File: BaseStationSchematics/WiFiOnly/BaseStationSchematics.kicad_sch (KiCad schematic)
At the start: 9 parts, among them U1 DOIT-ESP32-DEVKIT-V1, U2 Ra01_Breakout_Module-Ra01_Bre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, U3 LM386N based audio amplifier

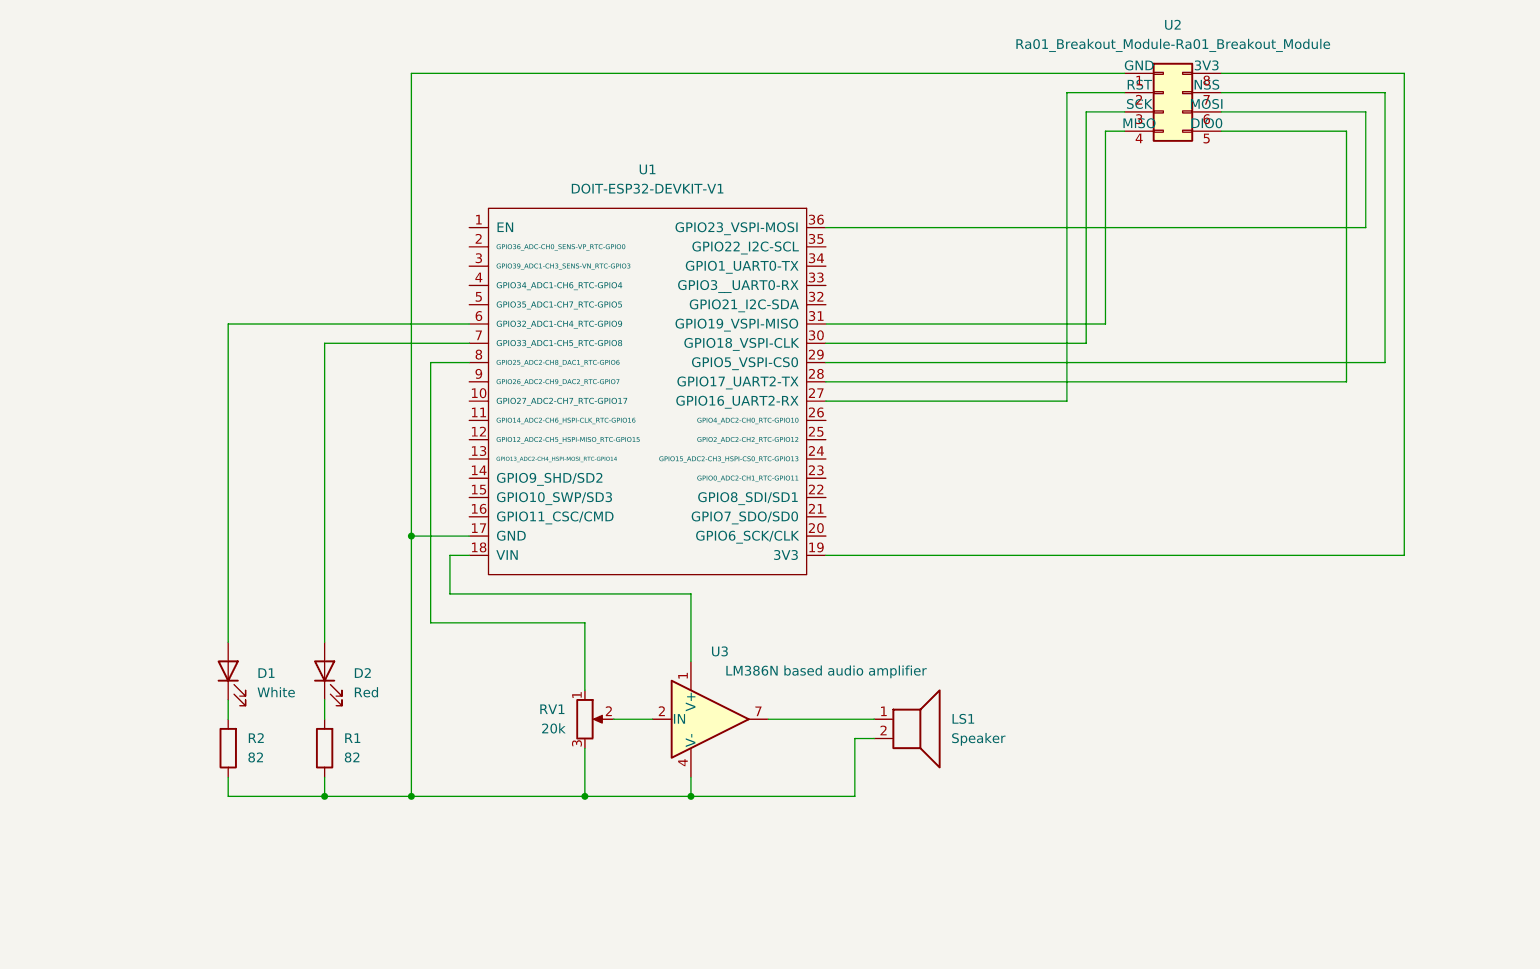
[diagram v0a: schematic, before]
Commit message: Added barometer and local timeseries
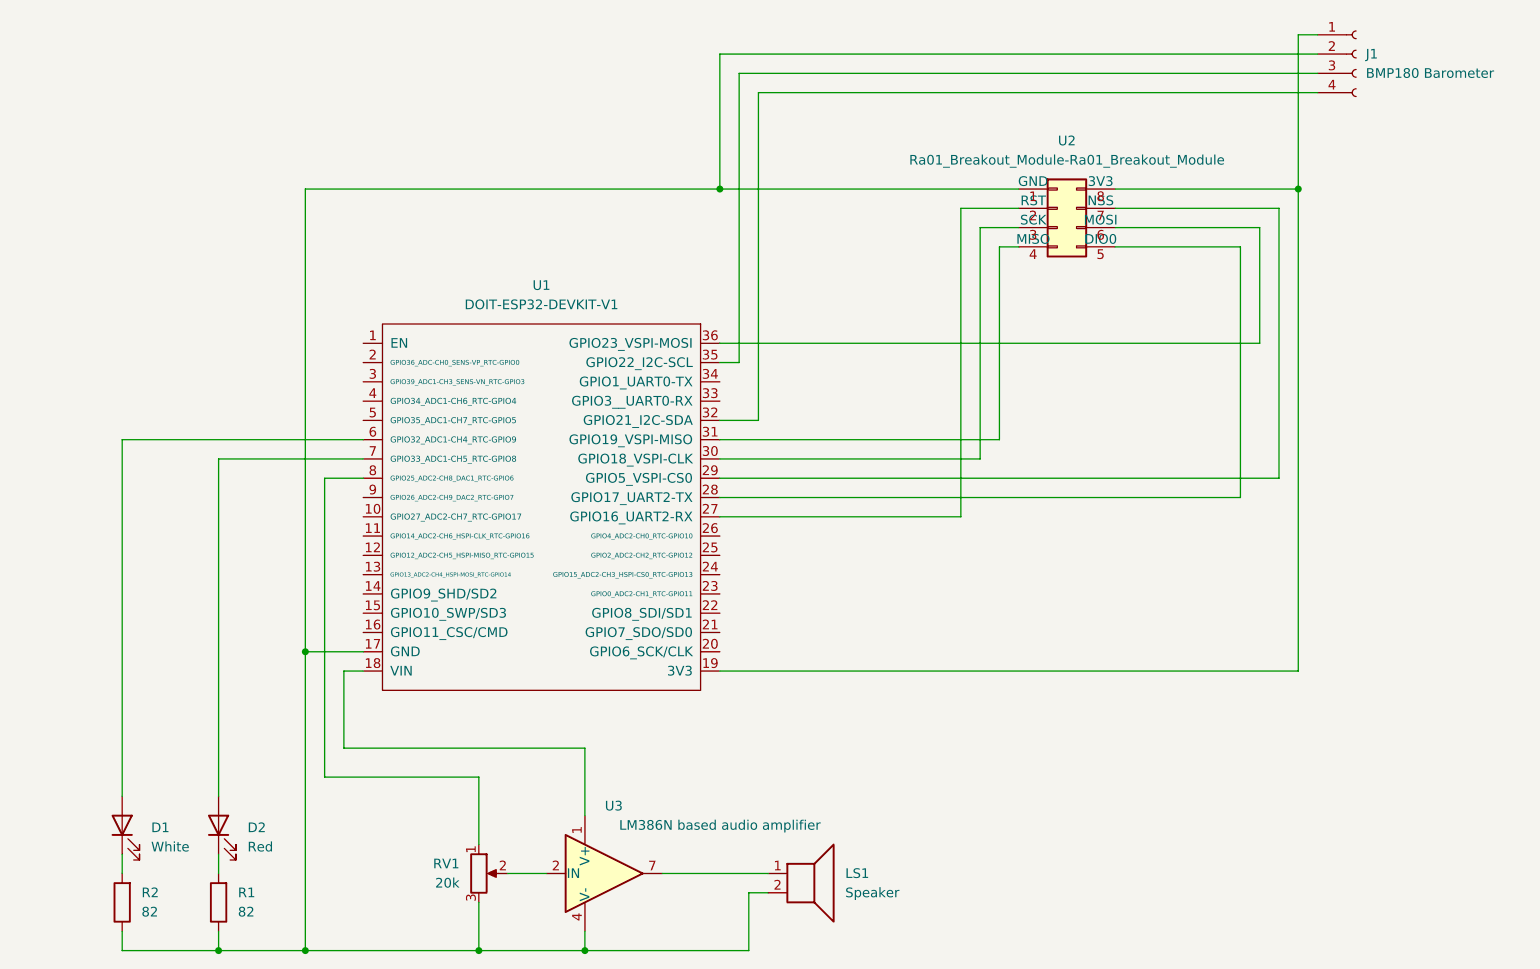
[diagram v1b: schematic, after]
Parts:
- added J1: BMP180 Barometer, symbol Connector:Conn_01x04_Socket
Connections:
- net at LS1.2, R1.1, R2.1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: now also J1.2 (Pin_2)
- net at U1.19 (3V3), U2.8 (3V3): now also J1.1 (Pin_1)
- net at U1.32 (GPIO21_I2C-SDA): now also J1.4 (Pin_4)
- net at U1.35 (GPIO22_I2C-SCL): now also J1.3 (Pin_3)
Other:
- moved on the sheet: D1, D2, LS1, R1, R2, RV1, U1, U2, U3

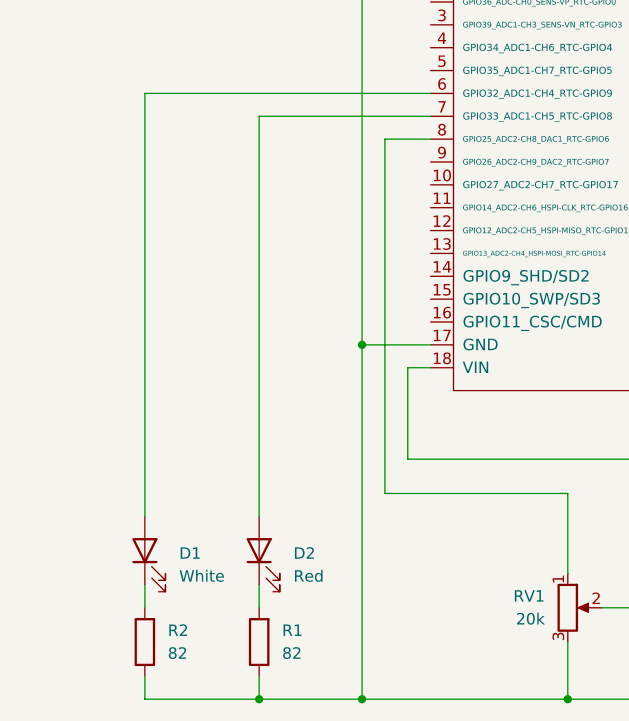
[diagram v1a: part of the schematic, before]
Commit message: Started to implement air conditioner IR, printing reset reason and time to attribute.
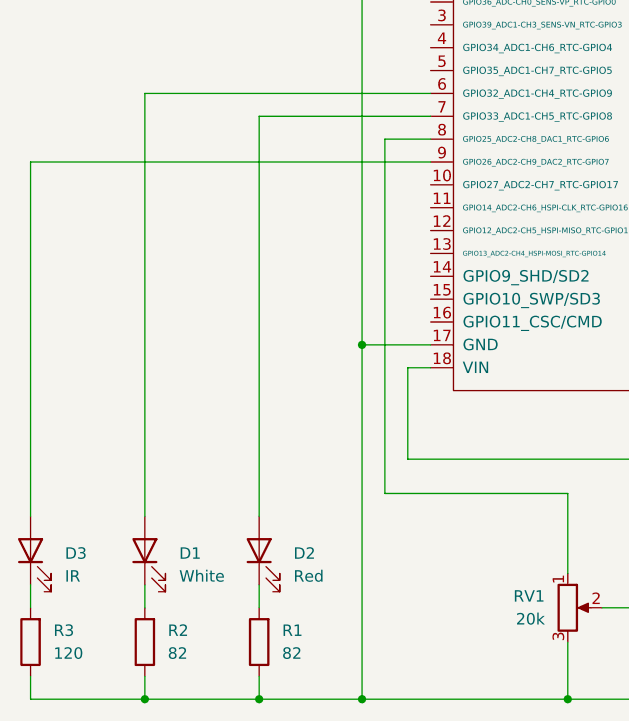
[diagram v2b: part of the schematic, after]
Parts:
- added D3: IR, symbol Device:LED
- added R3: 120, symbol Device:R
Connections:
- net at J1.2 (Pin_2), LS1.2, R1.1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: now also R3.1
- net at U1.9 (GPIO26_ADC2-CH9_DAC2_RTC-GPIO7): now also D3.2 (A)
- new net: D3.1 (K), R3.2
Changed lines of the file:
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@@
+	)
+	(junction
+		(at 63.5 160.02)
+		(diameter 0)
+		(color 0 0 0 0)
 	)
 	(junction
@@
 	(wire
 		(pts
+			(xy 50.8 157.48) (xy 50.8 160.02)
+		)
+		(stroke
+			(width 0)
+			(type default)
+		)
+	)
+	(wire
+		(pts
 			(xy 179.07 92.71) (xy 142.24 92.71)
 		)
@@
 	(wire
 		(pts
+			(xy 50.8 160.02) (xy 63.5 160.02)
+		)
+		(stroke
+			(width 0)
+			(type default)
+		)
+	)
+	(wire
+		(pts
 			(xy 142.24 97.79) (xy 215.9 97.79)
 		)
@@
 	(wire
 		(pts
+			(xy 50.8 100.33) (xy 95.25 100.33)
+		)
+		(stroke
+			(width 0)
+			(type default)
+		)
+	)
+	(wire
+		(pts
 			(xy 87.63 59.69) (xy 142.24 59.69)
 		)
@@
 	(wire
 		(pts
+			(xy 50.8 139.7) (xy 50.8 100.33)
+		)
+		(stroke
+			(width 0)
+			(type default)
+		)
+	)
+	(wire
+		(pts
 			(xy 215.9 97.79) (xy 215.9 62.23)
 		)
@@
 	(wire
 		(pts
+			(xy 50.8 147.32) (xy 50.8 149.86)
+		)
+		(stroke
+			(width 0)
+			(type default)
+		)
+	)
+	(wire
+		(pts
 			(xy 90.17 137.16) (xy 90.17 97.79)
 		)
@@
 			(width 0)
 			(type default)
+		)
+	)
+	(symbol
+		(lib_id "Device:LED")
+		(at 50.8 143.51 90)
+		(unit 1)
+		(exclude_from_sim no)
+		(in_bom yes)
+		(on_board yes)
+		(dnp no)
+		(fields_autoplaced yes)
+		(property "Reference" "D3"
+			(at 54.61 143.8274 90)
+			(effects
+				(font
+					(size 1.27 1.27)
+				)
+				(justify right)
+			)
+		)
+		(property "Value" "IR"
+			(at 54.61 146.3674 90)
+			(effects
+				(font
+					(size 1.27 1.27)
+				)
+				(justify right)
+			)
+		)
+		(property "Footprint" ""
+			(at 50.8 143.51 0)
+			(effects
+				(font
+					(size 1.27 1.27)
+				)
+				(hide yes)
+			)
+		)
+		(property "Datasheet" "~"
+			(at 50.8 143.51 0)
+			(effects
+				(font
+					(size 1.27 1.27)
+				)
+				(hide yes)
+			)
+		)
+		(property "Description" ""
+			(at 50.8 143.51 0)
+			(effects
+				(font
+					(size 1.27 1.27)
+				)
+				(hide yes)
+			)
+		)
+		(pin "1"
+		)
+		(pin "2"
+		)
+		(instances
+			(project "BaseStationSchematics"
+				(path "/5e1c3aec-ae2c-4561-b8d9-09ecd3197e65"
+					(reference "D3")
+					(unit 1)
+				)
+			)
 		)
 	)
@@
 					(unit 1)
 				)
+			)
+		)
+	)
+	(symbol
+		(lib_id "Device:R")
+		(at 50.8 153.67 180)
+		(unit 1)
+		(exclude_from_sim no)
+		(in_bom yes)
+		(on_board yes)
+		(dnp no)
+		(fields_autoplaced yes)
+		(property "Reference" "R3"
+			(at 53.34 152.3999 0)
+			(effects
+				(font
+					(size 1.27 1.27)
+				)
+				(justify right)
+			)
+		)
+		(property "Value" "120"
+			(at 53.34 154.9399 0)
+			(effects
+				(font
+					(size 1.27 1.27)
+				)
+				(justify right)
+			)
+		)
+		(property "Footprint" ""
+			(at 52.578 153.67 90)
+			(effects
+				(font
+					(size 1.27 1.27)
+				)
+				(hide yes)
+			)
+		)
+		(property "Datasheet" "~"
+			(at 50.8 153.67 0)
+			(effects
+				(font
+					(size 1.27 1.27)
+				)
+				(hide yes)
+			)
+		)
+		(property "Description" ""
+			(at 50.8 153.67 0)
+			(effects
+				(font
+					(size 1.27 1.27)
+				)
+				(hide yes)
+			)
+		)
+		(pin "1"
+		)
+		(pin "2"
+		)
+		(instances
+			(project "BaseStationSchematics"
+				(path "/5e1c3aec-ae2c-4561-b8d9-09ecd3197e65"
+					(reference "R3")
+					(unit 1)
+				)
